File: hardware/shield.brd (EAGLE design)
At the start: 68.6 x 53.3 mm, 7 parts, among them U1 ARDUINOR3-DIMENSION, X1 22-23-2021

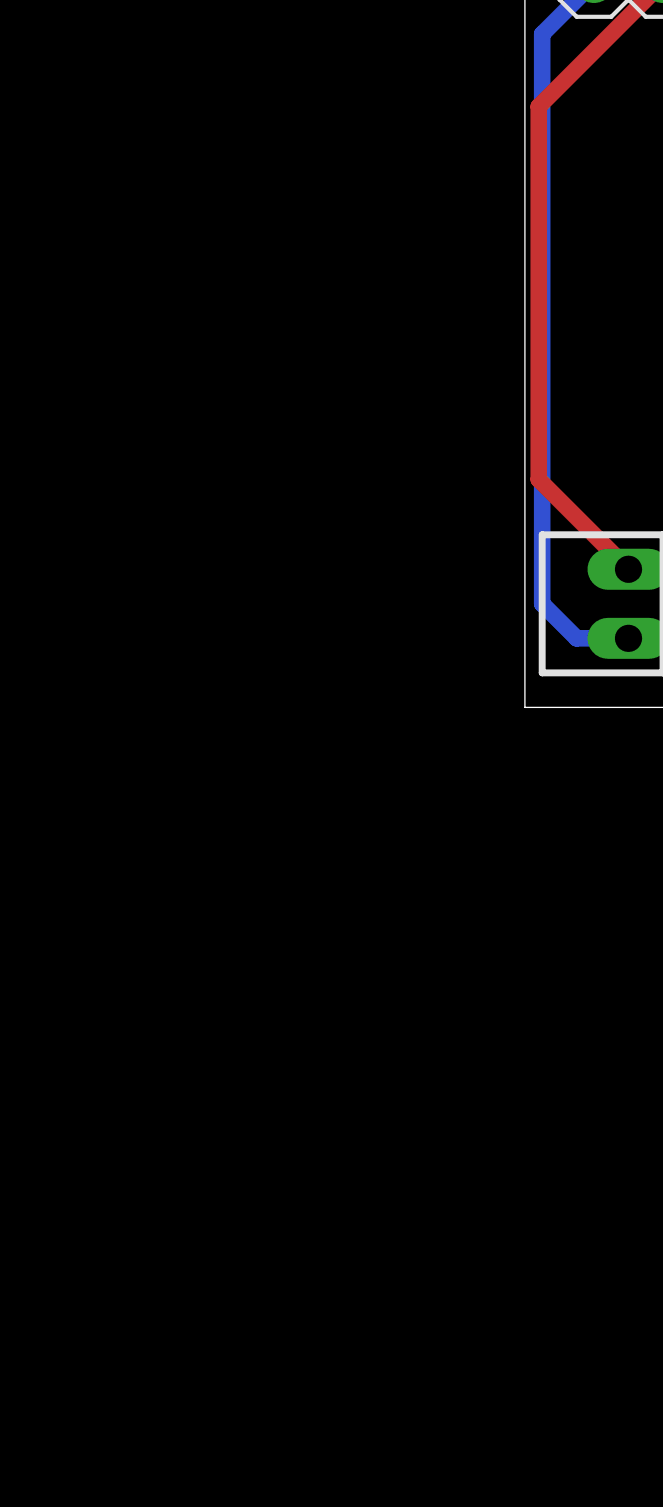
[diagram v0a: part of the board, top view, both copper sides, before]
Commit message: add bluetoothdevice to schematic
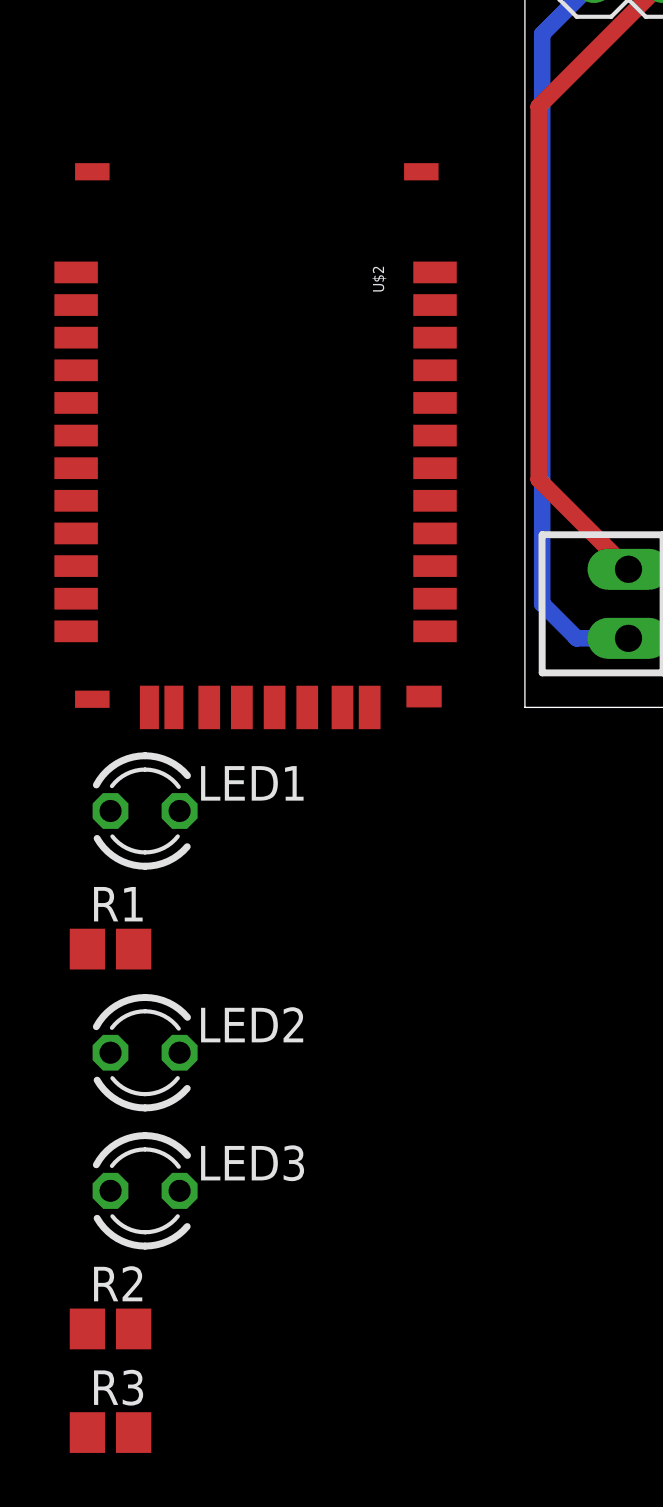
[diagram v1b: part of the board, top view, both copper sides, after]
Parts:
- added LED1, LED2, LED3: (no value), led:LED3MM
- added R1: (no value), resistor:R0805
- added R2, R3: 220, resistor:R0805
- added U$2: BLUETOOTH-RN42, RN4x:RN42
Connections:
- removed net 3V: U1.3V
- new net +3V3: LED3.A, U$2.11, U1.3V
- new net BTCONNECTED: R2.1, U$2.19
- new net BTRESET: U$2.5
- new net N$2: LED1.A, R1.1
- new net N$3: LED1.K, U1.D13
- new net N$5: LED2.A, R2.2
- new net N$7: LED3.K, R3.2
- new net N$8: R3.1, U$2.21
- new net RX: U1.D0
- new net TX: U1.D1
- net +5V: now also R1.2
- net GND: now also LED2.K, U$2.1, U$2.12, U$2.28, U$2.29, U$2.36, U$2.37, U$2.38, U$2.39
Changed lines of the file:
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@@
 </element>
 <element name="JP3" library="adafruit" package="2X04" value="" x="3.81" y="40.64" rot="R90"/>
+<element name="U$2" library="RN4x" package="RN42" value="BLUETOOTH-RN42" x="-16.51" y="0"/>
+<element name="LED1" library="led" package="LED3MM" value="" x="-13.97" y="-3.81"/>
+<element name="R1" library="resistor" package="R0805" value="" x="-15.24" y="-8.89"/>
+<element name="LED2" library="led" package="LED3MM" value="" x="-13.97" y="-12.7"/>
+<element name="LED3" library="led" package="LED3MM" value="" x="-13.97" y="-17.78"/>
+<element name="R2" library="resistor" package="R0805" value="220" x="-15.24" y="-22.86"/>
+<element name="R3" library="resistor" package="R0805" value="220" x="-15.24" y="-26.67"/>
 </elements>
 <signals>
-<signal name="3V">
-<contactref element="U1" pad="3V"/>
-</signal>
 <signal name="N$1">
 <contactref element="U1" pad="A0"/>
@@
 <wire x1="63.5" y1="45.72" x2="63.5" y2="13.97" width="0.6096" layer="16"/>
 <wire x1="63.5" y1="13.97" x2="60.96" y2="11.43" width="0.6096" layer="16"/>
+<contactref element="U$2" pad="1"/>
+<contactref element="U$2" pad="12"/>
+<contactref element="U$2" pad="28"/>
+<contactref element="U$2" pad="29"/>
+<contactref element="U$2" pad="36"/>
+<contactref element="U$2" pad="37"/>
+<contactref element="U$2" pad="38"/>
+<contactref element="U$2" pad="39"/>
+<contactref element="LED2" pad="K"/>
+<wire x1="-12.91" y1="0" x2="-12.7" y2="-12.7" width="0" layer="19" extent="1-1"/>
+<wire x1="-15.91" y1="0.3" x2="-12.91" y2="0" width="0" layer="19" extent="1-1"/>
+<wire x1="-16.506" y1="2.798" x2="-15.91" y2="0.3" width="0" layer="19" extent="1-1"/>
+<wire x1="-6.71" y1="-0.002" x2="-12.91" y2="0" width="0" layer="19" extent="1-1"/>
+<wire x1="-3.71" y1="0.4" x2="-6.71" y2="-0.002" width="0" layer="19" extent="1-1"/>
+<wire x1="0.635" y1="3.81" x2="-3.71" y2="0.4" width="0" layer="19" extent="1-16"/>
+<wire x1="-3.81" y1="19.7" x2="0.635" y2="24.765" width="0" layer="19" extent="1-16"/>
+<wire x1="-15.91" y1="19.7" x2="-3.81" y2="19.7" width="0" layer="19" extent="1-1"/>
+<wire x1="-16.506" y1="15.998" x2="-15.91" y2="19.7" width="0" layer="19" extent="1-1"/>
 </signal>
 <signal name="N$4">
@@
 <wire x1="63.5" y1="11.43" x2="60.96" y2="13.97" width="0.6096" layer="1"/>
 <wire x1="60.96" y1="13.97" x2="60.96" y2="39.37" width="0.6096" layer="1"/>
+<contactref element="R1" pad="2"/>
+<wire x1="-14.39" y1="-8.89" x2="38.1" y2="2.54" width="0" layer="19" extent="1-1"/>
 </signal>
 <signal name="DRIVE_L">
@@
 <wire x1="5.08" y1="26.67" x2="5.08" y2="31.75" width="0.6096" layer="1"/>
 </signal>
+<signal name="RX">
+<contactref element="U1" pad="D0"/>
+</signal>
+<signal name="TX">
+<contactref element="U1" pad="D1"/>
+</signal>
+<signal name="N$2">
+<contactref element="R1" pad="1"/>
+<contactref element="LED1" pad="A"/>
+<wire x1="-15.24" y1="-3.81" x2="-16.09" y2="-8.89" width="0" layer="19" extent="1-1"/>
+</signal>
+<signal name="N$3">
+<contactref element="LED1" pad="K"/>
+<contactref element="U1" pad="D13"/>
+<wire x1="-12.7" y1="-3.81" x2="28.956" y2="50.8" width="0" layer="19" extent="1-1"/>
+</signal>
+<signal name="BTCONNECTED">
+<contactref element="U$2" pad="19"/>
+<contactref element="R2" pad="1"/>
+<wire x1="-3.306" y1="9.998" x2="-16.09" y2="-22.86" width="0" layer="19" extent="1-1"/>
+</signal>
+<signal name="+3V3">
+<contactref element="U1" pad="3V"/>
+<contactref element="LED3" pad="A"/>
+<contactref element="U$2" pad="11"/>
+<wire x1="-16.506" y1="3.998" x2="35.56" y2="2.54" width="0" layer="19" extent="1-1"/>
+<wire x1="-15.24" y1="-17.78" x2="-16.506" y2="3.998" width="0" layer="19" extent="1-1"/>
+</signal>
+<signal name="N$5">
+<contactref element="R2" pad="2"/>
+<contactref element="LED2" pad="A"/>
+<wire x1="-15.24" y1="-12.7" x2="-14.39" y2="-22.86" width="0" layer="19" extent="1-1"/>
+</signal>
+<signal name="N$7">
+<contactref element="R3" pad="2"/>
+<contactref element="LED3" pad="K"/>
+<wire x1="-12.7" y1="-17.78" x2="-14.39" y2="-26.67" width="0" layer="19" extent="1-1"/>
+</signal>
+<signal name="N$8">
+<contactref element="R3" pad="1"/>
+<contactref element="U$2" pad="21"/>
+<wire x1="-3.306" y1="12.398" x2="-16.09" y2="-26.67" width="0" layer="19" extent="1-1"/>
+</signal>
+<signal name="BTRESET">
+<contactref element="U$2" pad="5"/>
+</signal>
 </signals>
